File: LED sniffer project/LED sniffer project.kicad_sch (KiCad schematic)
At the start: 4 parts

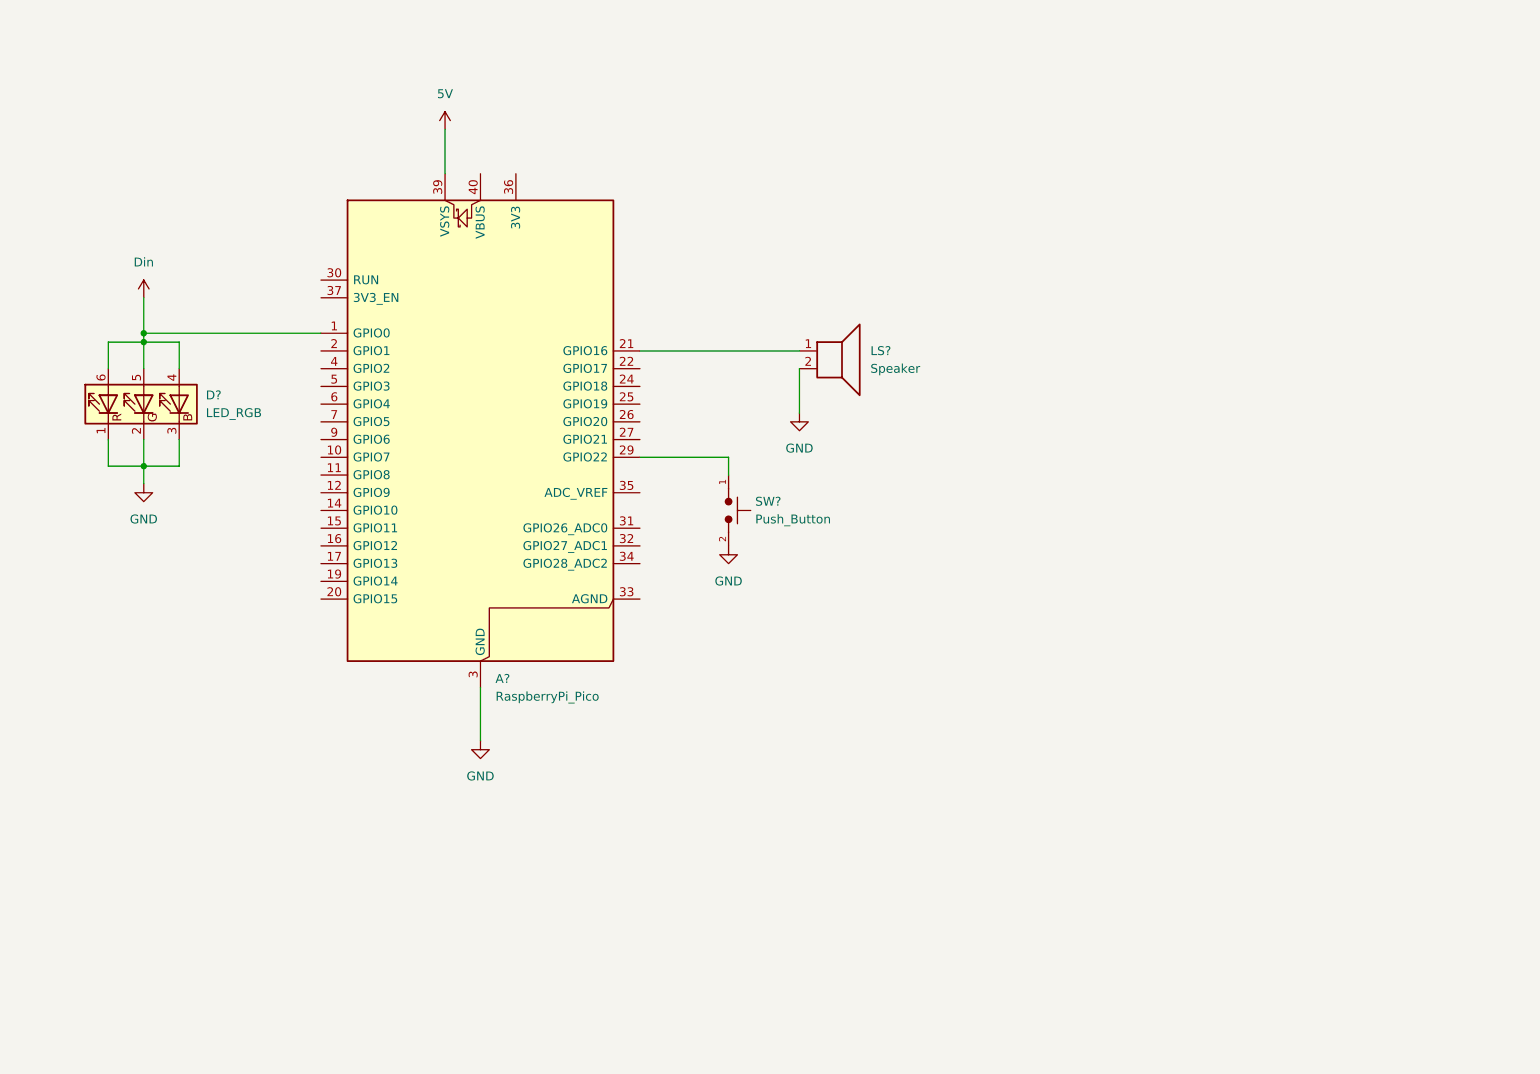
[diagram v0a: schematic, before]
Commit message: Updated Schematic to Revision 2
This was designed for building the breadboard under my understanding of the demonstration set up requirements communicated at our team meeting on 11/4/2025
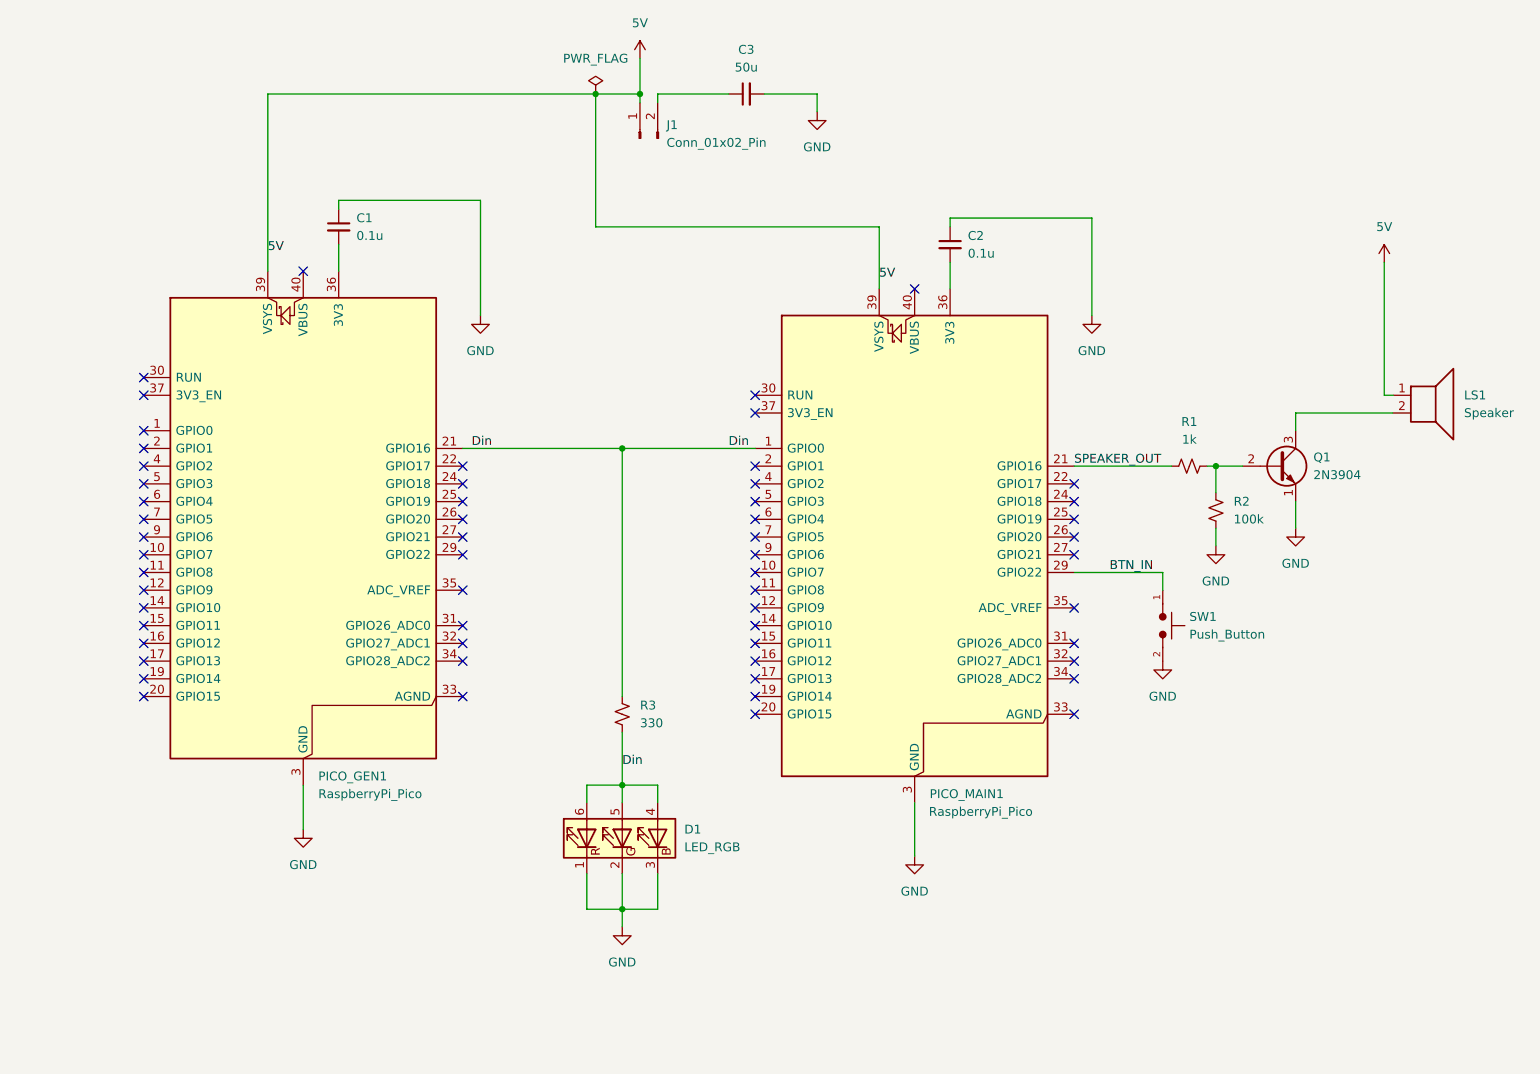
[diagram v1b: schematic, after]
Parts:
- added C1, C2: 0.1u, symbol Device:C_Small
- added C3: 50u, symbol Device:C_Small
- added J1: Conn_01x02_Pin, symbol Connector:Conn_01x02_Pin
- added PICO_GEN1: RaspberryPi_Pico, Module:RaspberryPi_Pico_Common_Unspecified, symbol MCU_Module:RaspberryPi_Pico
- added Q1: 2N3904, Package_TO_SOT_THT:TO-92_Inline, symbol Transistor_BJT:2N3904
- added R1: 1k, symbol Device:R_Small_US
- added R2: 100k, symbol Device:R_Small_US
- added R3: 330, symbol Device:R_Small_US
- gave numbers to parts that had none: 4
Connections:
- net 5V: now also LS1.1, J1.1 (Pin_1), PICO_GEN1.39 (VSYS)
- net Din: now also PICO_GEN1.21 (GPIO16), R3.1, R3.2
- net GND: now also C1.1, C2.1, C3.2, PICO_GEN1.13 (GND), PICO_GEN1.18 (GND), PICO_GEN1.23 (GND), PICO_GEN1.28 (GND), PICO_GEN1.3 (GND), PICO_GEN1.38 (GND), PICO_GEN1.8 (GND), Q1.1 (E), R2.1; no longer LS1.2
- net SPEAKER_OUT: now reaches PICO_MAIN1.21 (GPIO16)
- net SPEAKER_OUT: now also R1.1; no longer LS1.1
- net BTN_IN: now reaches PICO_MAIN1.29 (GPIO22), SW1.1
- net at PICO_MAIN1.36 (3V3): now also C2.2
- new net: Q1.2 (B), R1.2, R2.2
- new net: LS1.2, Q1.3 (C)
- new net: C3.1, J1.2 (Pin_2)
- new net: C1.2, PICO_GEN1.36 (3V3)
- no-connect marks 0 -> 58
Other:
- title: (none) -> LED Sniffer Project
- moved on the sheet: D1, LS1, PICO_MAIN1, SW1

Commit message: HW6 updated schematic (revision 2), initial layout, and 3D render
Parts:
- C1, C2, C3: footprint (none) -> Capacitor_SMD:C_1206_3216Metric
- D1: footprint (none) -> LED_SMD:LED_RGB_PLCC-6
- J1, LS1: footprint (none) -> Connector_PinHeader_2.54mm:PinHeader_1x02_P2.54mm_Vertical
- R1, R2, R3: footprint (none) -> Resistor_SMD:R_1206_3216Metric
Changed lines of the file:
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@@
 			)
 		)
-		(property "Footprint" ""
+		(property "Footprint" "Connector_PinHeader_2.54mm:PinHeader_1x02_P2.54mm_Vertical"
 			(at 137.16 38.1 0)
 			(effects
@@
 			)
 		)
-		(property "Footprint" ""
+		(property "Footprint" "Resistor_SMD:R_1206_3216Metric"
 			(at 215.9 85.09 0)
 			(effects
@@
 			)
 		)
-		(property "Footprint" ""
+		(property "Footprint" "Resistor_SMD:R_1206_3216Metric"
 			(at 134.62 120.65 0)
 			(effects
@@
 			)
 		)
-		(property "Footprint" ""
+		(property "Footprint" "Capacitor_SMD:C_1206_3216Metric"
 			(at 93.98 50.8 0)
 			(effects
@@
 			)
 		)
-		(property "Footprint" ""
+		(property "Footprint" "Capacitor_SMD:C_1206_3216Metric"
 			(at 181.61 53.34 0)
 			(effects
@@
 			)
 		)
-		(property "Footprint" ""
+		(property "Footprint" "LED_SMD:LED_RGB_PLCC-6"
 			(at 135.89 138.43 0)
 			(effects
@@
 			)
 		)
-		(property "Footprint" ""
+		(property "Footprint" "Capacitor_SMD:C_1206_3216Metric"
 			(at 152.4 31.75 0)
 			(effects
@@
 			)
 		)
-		(property "Footprint" ""
+		(property "Footprint" "Connector_PinHeader_2.54mm:PinHeader_1x02_P2.54mm_Vertical"
 			(at 250.19 80.01 0)
 			(effects
@@
 			)
 		)
-		(property "Footprint" ""
+		(property "Footprint" "Resistor_SMD:R_1206_3216Metric"
 			(at 219.71 91.44 0)
 			(effects

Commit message: rough draft of schematic
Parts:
- removed C1, C2: 0.1u, Capacitor_SMD:C_1206_3216Metric, symbol Device:C_Small
- removed C3: 50u, Capacitor_SMD:C_1206_3216Metric, symbol Device:C_Small
- removed D1: LED_RGB, LED_SMD:LED_RGB_PLCC-6, symbol Device:LED_RGB
- removed J1: Conn_01x02_Pin, Connector_PinHeader_2.54mm:PinHeader_1x02_P2.54mm_Vertical, symbol Connector:Conn_01x02_Pin
- removed LS1: Speaker, Connector_PinHeader_2.54mm:PinHeader_1x02_P2.54mm_Vertical, symbol Device:Speaker
- removed PICO_GEN1: RaspberryPi_Pico, Module:RaspberryPi_Pico_Common_Unspecified, symbol MCU_Module:RaspberryPi_Pico
- removed Q1: 2N3904, Package_TO_SOT_THT:TO-92_Inline, symbol Transistor_BJT:2N3904
- removed R1: 1k, Resistor_SMD:R_1206_3216Metric, symbol Device:R_Small_US
- removed R2: 100k, Resistor_SMD:R_1206_3216Metric, symbol Device:R_Small_US
- removed R3: 330, Resistor_SMD:R_1206_3216Metric, symbol Device:R_Small_US
- added J1: Conn_01x02, Connector_PinHeader_1.00mm:PinHeader_1x02_P1.00mm_Vertical, symbol PCM_4ms_Connector:Conn_01x02
- added J2: Conn_01x03, Connector_PinHeader_1.00mm:PinHeader_1x03_P1.00mm_Vertical, symbol PCM_4ms_Connector:Conn_01x03
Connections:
- net 5V: now also J2.1 (Pin_1)
- net GND: now also J1.2 (Pin_2), J2.3 (Pin_3)
- net at PICO_MAIN1.34 (GPIO28_ADC2): now also J2.2 (Pin_2)
- net Din: no longer names the net of PICO_MAIN1.1 (GPIO0)
- net SPEAKER_OUT: no longer names the net of PICO_MAIN1.21 (GPIO16)
- net SPEAKER_OUT: now also J1.1 (Pin_1)
- no-connect marks 58 -> 30

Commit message: Updated with a slightly less rough draft
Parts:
- added D1: SK6812, LED_SMD:LED_SK6812_PLCC4_5.0x5.0mm_P3.2mm, symbol LED:SK6812
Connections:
- net 5V: now also D1.3 (VDD)
- net GND: now also D1.1 (VSS)
- net at J2.2 (Pin_2), PICO_MAIN1.34 (GPIO28_ADC2): now also D1.2 (DIN)
- no-connect marks 30 -> 31
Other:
- company: (none) -> Team 09
- moved on the sheet: J1, J2, PICO_MAIN1, SW1

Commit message: Updated CAD
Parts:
- added J3: Conn_01x03, Connector_PinHeader_2.54mm:PinHeader_1x03_P2.54mm_Vertical, symbol PCM_4ms_Connector:Conn_01x03
- added J4, J5: Conn_01x04, Connector_PinHeader_2.54mm:PinHeader_1x04_P2.54mm_Vertical, symbol PCM_4ms_Connector:Conn_01x04
- added R1: 22k, Resistor_THT:R_Axial_DIN0207_L6.3mm_D2.5mm_P10.16mm_Horizontal, symbol PCM_SL_Resistors:22k
- added R2: 33k, Resistor_THT:R_Axial_DIN0207_L6.3mm_D2.5mm_P10.16mm_Horizontal, symbol PCM_SL_Resistors:33k
- J1: footprint Connector_PinHeader_1.00mm:PinHeader_1x02_P1.00mm_Vertical -> Connector_PinHeader_2.54mm:PinHeader_1x02_P2.54mm_Vertical
- J2: footprint Connector_PinHeader_1.00mm:PinHeader_1x03_P1.00mm_Vertical -> Connector_PinHeader_2.54mm:PinHeader_1x03_P2.54mm_Vertical
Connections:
- net 5V: now also J5.1 (Pin_1)
- net GND: now also J3.3 (Pin_3), J4.4 (Pin_4), J5.4 (Pin_4), R2.1
- net at J1.1 (Pin_1), PICO_MAIN1.21 (GPIO16): now also J3.1 (Pin_1), J4.1 (Pin_1)
- net at PICO_MAIN1.22 (GPIO17): now also J3.2 (Pin_2), J4.2 (Pin_2)
- net at PICO_MAIN1.24 (GPIO18): now also J4.3 (Pin_3)
- net at PICO_MAIN1.32 (GPIO27_ADC1): now also R1.1, R2.2
- net at D1.2 (DIN), J2.2 (Pin_2): now also J5.2 (Pin_2), R1.2; no longer PICO_MAIN1.34 (GPIO28_ADC2)
- new net: J5.3 (Pin_3), PICO_MAIN1.34 (GPIO28_ADC2)
- no-connect marks 31 -> 27
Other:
- note added: "Input Connectors"
- note added: "Output Connectors"
- moved on the sheet: D1, J1, J2, SW1

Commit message: Slight update
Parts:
- added R3: 22k, Resistor_SMD:R_0603_1608Metric, symbol PCM_SL_Resistors:22k
- added R4: 33k, Resistor_SMD:R_0603_1608Metric, symbol PCM_SL_Resistors:33k
- R1, R2: footprint Resistor_THT:R_Axial_DIN0207_L6.3mm_D2.5mm_P10.16mm_Horizontal -> Resistor_SMD:R_0603_1608Metric
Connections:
- net GND: now also R4.1
- net at PICO_MAIN1.34 (GPIO28_ADC2): now also R3.1, R4.2; no longer J5.3 (Pin_3)
- new net: J5.3 (Pin_3), R3.2

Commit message: Possible submission
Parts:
- added J6: Conn_01x04, Connector_PinHeader_2.54mm:PinHeader_1x04_P2.54mm_Vertical, symbol PCM_4ms_Connector:Conn_01x04
- renumbered J2 to J1, J5 to J2, J1 to J3, J3 to J4, J4 to J5
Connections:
- net GND: now also J6.1 (Pin_1)
- net at PICO_MAIN1.17 (GPIO13): now also J6.4 (Pin_4)
- net at PICO_MAIN1.19 (GPIO14): now also J6.3 (Pin_3)
- net at PICO_MAIN1.20 (GPIO15): now also J6.2 (Pin_2)
- net at J3.1 (Pin_1), J4.1 (Pin_1), J5.1 (Pin_1): now also PICO_MAIN1.24 (GPIO18); no longer PICO_MAIN1.21 (GPIO16)
- net at J4.2 (Pin_2), J5.2 (Pin_2): now also PICO_MAIN1.25 (GPIO19); no longer PICO_MAIN1.22 (GPIO17)
- net at J5.3 (Pin_3): now also PICO_MAIN1.26 (GPIO20); no longer PICO_MAIN1.24 (GPIO18)
- net at R1.1, R2.2: now also PICO_MAIN1.21 (GPIO16); no longer PICO_MAIN1.32 (GPIO27_ADC1)
- net at R3.1, R4.2: now also PICO_MAIN1.22 (GPIO17); no longer PICO_MAIN1.34 (GPIO28_ADC2)
- net BTN_IN: no longer names the net of PICO_MAIN1.29 (GPIO22)
- net BTN_IN: no longer SW1.1
- new net: PICO_MAIN1.34 (GPIO28_ADC2), SW1.1
- no-connect marks 27 -> 24
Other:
- note added: "Input Connectors Can accept 1 or 2 data streams"
- note added: "Output Connectors Option to drive output with 1, 2, or 3 GPIO pins"
- note added: "Pattern Recognition Switch"
- note added: "Redundant connector"
- note removed: "Input Connectors"
- note removed: "Output Connectors"
- moved on the sheet: D1, J1, J2, J3, J4, J5, PICO_MAIN1, R1, R2, R3, R4, SW1

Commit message: Final Cad
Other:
- note added: "Redundancy connector for alternate approach"
- note removed: "Redundant connector"
- moved on the sheet: J6
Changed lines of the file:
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@@
 	)
 	(rectangle
-		(start 49.53 132.08)
-		(end 73.66 149.86)
+		(start 48.26 121.92)
+		(end 76.2 147.32)
 		(stroke
 			(width 0)
@@
 	)
 	(rectangle
-		(start 184.15 86.36)
-		(end 217.17 119.38)
+		(start 185.42 83.82)
+		(end 218.44 119.38)
 		(stroke
 			(width 0)
@@
 		)
 	)
-	(text "Output Connectors\nOption to drive output with 1, 2, or 3 GPIO pins\n"
+	(text "Output Connectors\nOption to drive output with 1, 2, \nor 3 GPIO pins\n"
 		(exclude_from_sim no)
-		(at 209.55 83.82 0)
+		(at 201.93 88.9 0)
 		(effects
 			(font
@@
 		)
 	)
-	(text "Redundant connector"
+	(text "Redundancy connector for\nalternate approach"
 		(exclude_from_sim no)
-		(at 60.96 134.62 0)
+		(at 62.23 124.46 0)
 		(effects
 			(font
@@
 	(wire
 		(pts
-			(xy 71.12 138.43) (xy 80.01 138.43)
-		)
-		(stroke
-			(width 0)
-			(type default)
-		)
-	)
-	(wire
-		(pts
 			(xy 205.74 106.68) (xy 205.74 113.03)
 		)
@@
 	(wire
 		(pts
-			(xy 71.12 143.51) (xy 80.01 143.51)
-		)
-		(stroke
-			(width 0)
-			(type default)
-		)
-	)
-	(wire
-		(pts
 			(xy 138.43 73.66) (xy 138.43 81.28)
 		)
@@
 	(wire
 		(pts
+			(xy 66.04 140.97) (xy 80.01 140.97)
+		)
+		(stroke
+			(width 0)
+			(type default)
+		)
+	)
+	(wire
+		(pts
 			(xy 149.86 73.66) (xy 149.86 66.04)
 		)
@@
 	(wire
 		(pts
-			(xy 71.12 146.05) (xy 77.47 146.05)
-		)
-		(stroke
-			(width 0)
-			(type default)
-		)
-	)
-	(wire
-		(pts
 			(xy 125.73 138.43) (xy 132.08 138.43)
 		)
@@
 	(wire
 		(pts
+			(xy 63.5 143.51) (xy 63.5 138.43)
+		)
+		(stroke
+			(width 0)
+			(type default)
+		)
+	)
+	(wire
+		(pts
 			(xy 208.28 115.57) (xy 198.12 115.57)
 		)
@@
 	(wire
 		(pts
+			(xy 68.58 138.43) (xy 80.01 138.43)
+		)
+		(stroke
+			(width 0)
+			(type default)
+		)
+	)
+	(wire
+		(pts
 			(xy 153.67 73.66) (xy 149.86 73.66)
 		)
@@
 	(wire
 		(pts
+			(xy 60.96 146.05) (xy 60.96 138.43)
+		)
+		(stroke
+			(width 0)
+			(type default)
+		)
+	)
+	(wire
+		(pts
 			(xy 208.28 106.68) (xy 208.28 115.57)
 		)
@@
 	(wire
 		(pts
+			(xy 66.04 140.97) (xy 66.04 138.43)
+		)
+		(stroke
+			(width 0)
+			(type default)
+		)
+	)
+	(wire
+		(pts
+			(xy 63.5 143.51) (xy 80.01 143.51)
+		)
+		(stroke
+			(width 0)
+			(type default)
+		)
+	)
+	(wire
+		(pts
 			(xy 125.73 110.49) (xy 173.99 110.49)
 		)
@@
 	(wire
 		(pts
-			(xy 71.12 140.97) (xy 80.01 140.97)
-		)
-		(stroke
-			(width 0)
-			(type default)
-		)
-	)
-	(wire
-		(pts
 			(xy 135.89 73.66) (xy 133.35 73.66)
+		)
+		(stroke
+			(width 0)
+			(type default)
+		)
+	)
+	(wire
+		(pts
+			(xy 60.96 146.05) (xy 77.47 146.05)
 		)
 		(stroke
@@
 	(symbol
 		(lib_id "PCM_4ms_Connector:Conn_01x04")
-		(at 66.04 143.51 180)
+		(at 63.5 133.35 90)
 		(unit 1)
 		(exclude_from_sim no)
@@
 		(dnp no)
 		(property "Reference" "J6"
-			(at 60.96 142.24 90)
+			(at 64.77 128.27 90)
 			(effects
 				(font
@@
 		)
 		(property "Value" "Conn_01x04"
-			(at 63.5 142.24 90)
+			(at 64.77 130.81 90)
 			(effects
 				(font
@@
 		)
 		(property "Footprint" "Connector_PinHeader_2.54mm:PinHeader_1x04_P2.54mm_Vertical"
-			(at 66.04 150.495 0)
+			(at 56.515 133.35 0)
 			(effects
 				(font
@@
 		)
 		(property "Datasheet" ""
-			(at 66.04 143.51 0)
+			(at 63.5 133.35 0)
 			(effects
 				(font
@@
 		)
 		(property "Description" "HEADER 1x4 MALE PINS 0.100” 180deg"
-			(at 66.04 143.51 0)
+			(at 63.5 133.35 0)
 			(effects
 				(font
@@
 		)
 		(property "Specifications" "HEADER 1x4 MALE PINS 0.100” 180deg"
-			(at 69.215 128.905 0)
+			(at 78.105 136.525 0)
 			(effects
 				(font
@@
 		)
 		(property "Manufacturer" "TAD"
-			(at 68.58 134.112 0)
+			(at 72.898 135.89 0)
 			(effects
 				(font
@@
 		)
 		(property "Part Number" "1-0401FBV0T"
-			(at 68.58 132.588 0)
-			(effects
-				(font
+			(at 74.422 135.89 0)
+			(effects
+				(font
